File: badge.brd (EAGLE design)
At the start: 90.7 x 92.4 mm, 178 parts, among them CN4 MicroUSB, IC3 MEGA8-AI, Q1 BSS138, Q2 BSS138, T1 MMUN2133LT1G, U1 TPS61090RSAR, U2 MCP73871, U3 LIS3DHTR, U4 MIC5225-3.3, Y1 16.00MHz

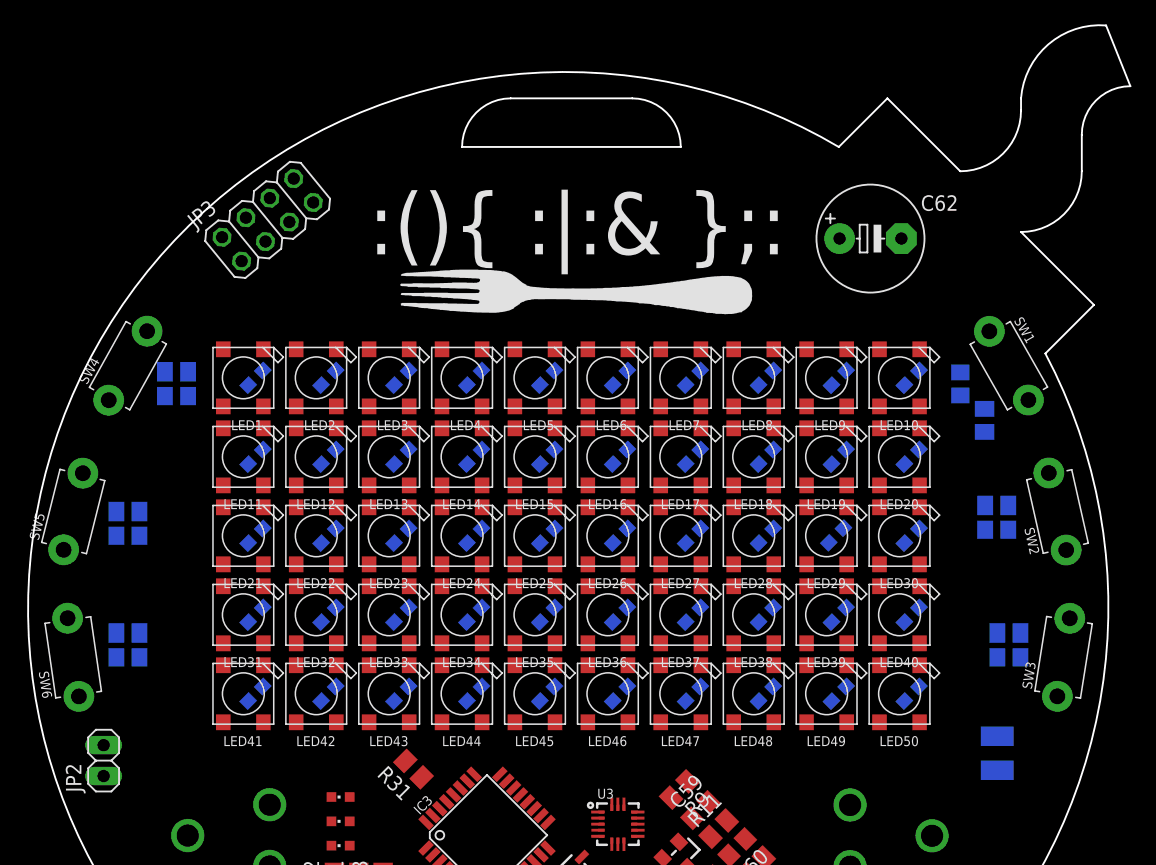
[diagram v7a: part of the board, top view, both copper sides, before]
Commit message: small silkscreen changes
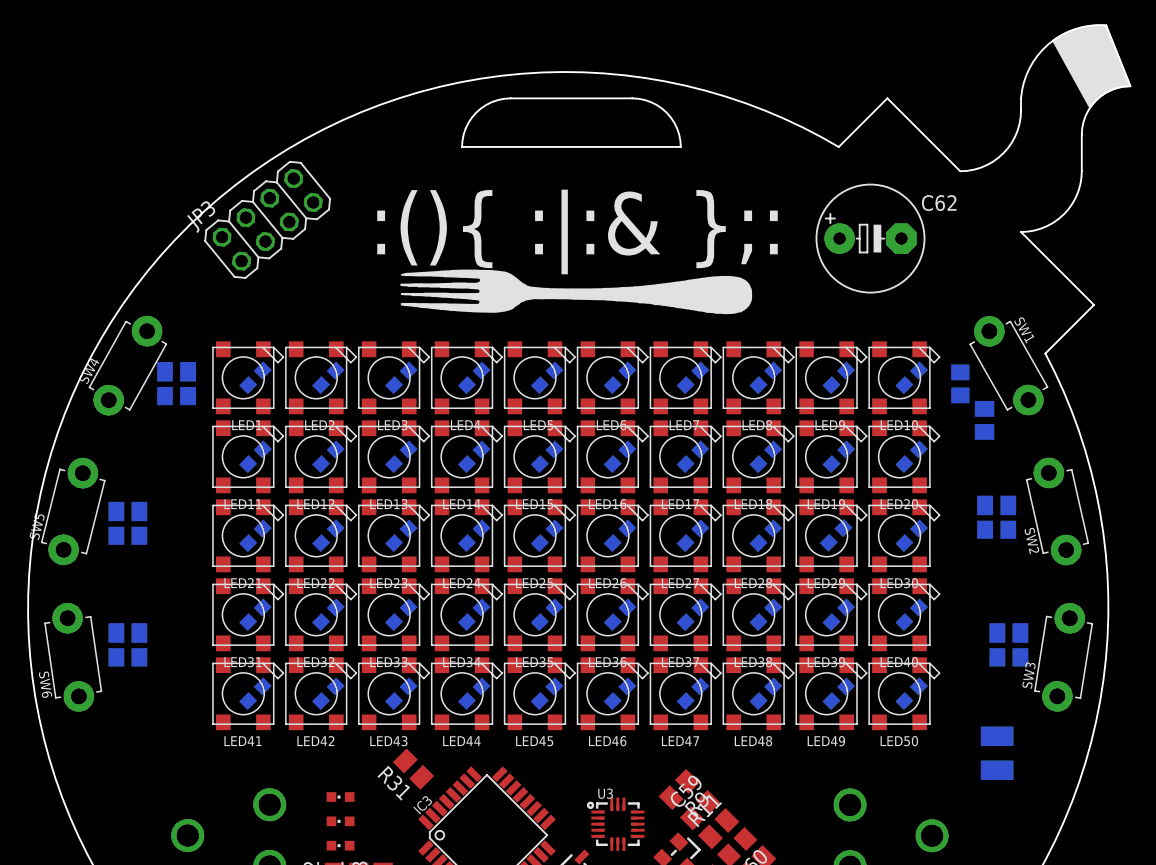
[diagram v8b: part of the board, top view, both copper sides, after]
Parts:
- removed JP2: PIEZO_HEADER, pinhead:1X02
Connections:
- net GND: no longer JP2.2
- net PIEZO: no longer JP2.1
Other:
- board text added: "fir3r007 ichorous videlen"
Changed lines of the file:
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@@
 <setting verticaltext="up"/>
 </settings>
-<grid distance="0.5" unitdist="mm" unit="mm" style="lines" multiple="1" display="yes" altdistance="5" altunitdist="mil" altunit="mil"/>
+<grid distance="0.000123031496" unitdist="mil" unit="mil" style="lines" multiple="1" display="yes" altdistance="5" altunitdist="mil" altunit="mil"/>
 <layers>
 <layer number="1" name="Top" color="4" fill="1" visible="yes" active="yes"/>
@@
 <dimension x1="0" y1="0" x2="100" y2="0" x3="50" y3="-6" textsize="1.778" layer="51"/>
 <dimension x1="100" y1="0" x2="100" y2="100" x3="105.5" y3="50" textsize="1.778" layer="51"/>
+<polygon width="0.1524" layer="21">
+<vertex x="90.002796875" y="92.986875"/>
+<vertex x="92.001878125" y="87.999740625"/>
+<vertex x="91.640853125" y="87.982459375"/>
+<vertex x="91.268303125" y="87.93445"/>
+<vertex x="90.8938375" y="87.846115625"/>
+<vertex x="90.52513125" y="87.71745"/>
+<vertex x="90.162184375" y="87.554221875"/>
+<vertex x="89.88565625" y="87.396753125"/>
+<vertex x="89.646340625" y="87.232959375"/>
+<vertex x="89.409496875" y="87.048928125"/>
+<vertex x="89.156653125" y="86.815284375"/>
+<vertex x="88.955015625" y="86.596046875"/>
+<vertex x="88.68296875" y="86.235984375"/>
+<vertex x="85.63738125" y="91.751709375"/>
+<vertex x="85.93680625" y="91.9585"/>
+<vertex x="86.259425" y="92.15668125"/>
+<vertex x="86.835534375" y="92.45165"/>
+<vertex x="87.411640625" y="92.67518125"/>
+<vertex x="87.893265625" y="92.81805625"/>
+<vertex x="88.289846875" y="92.908140625"/>
+<vertex x="88.76609375" y="92.975353125"/>
+<vertex x="89.288428125" y="93.015678125"/>
+<vertex x="89.732028125" y="93.015678125"/>
+<vertex x="90.002796875" y="92.996475"/>
+<vertex x="90.039284375" y="92.910059375"/>
+</polygon>
+<polygon width="0.1524" layer="22">
+<vertex x="89.978125" y="92.962203125"/>
+<vertex x="91.97720625" y="87.97506875"/>
+<vertex x="91.61618125" y="87.9577875"/>
+<vertex x="91.24363125" y="87.909778125"/>
+<vertex x="90.869165625" y="87.82144375"/>
+<vertex x="90.500459375" y="87.692778125"/>
+<vertex x="90.1375125" y="87.52955"/>
+<vertex x="89.860984375" y="87.37208125"/>
+<vertex x="89.62166875" y="87.2082875"/>
+<vertex x="89.384825" y="87.02425625"/>
+<vertex x="89.13198125" y="86.7906125"/>
+<vertex x="88.93034375" y="86.571375"/>
+<vertex x="88.658296875" y="86.2113125"/>
+<vertex x="85.612709375" y="91.7270375"/>
+<vertex x="85.912134375" y="91.933828125"/>
+<vertex x="86.234753125" y="92.132009375"/>
+<vertex x="86.8108625" y="92.426978125"/>
+<vertex x="87.38696875" y="92.650509375"/>
+<vertex x="87.86859375" y="92.793384375"/>
+<vertex x="88.265175" y="92.88346875"/>
+<vertex x="88.741421875" y="92.95068125"/>
+<vertex x="89.26375625" y="92.99100625"/>
+<vertex x="89.70735625" y="92.99100625"/>
+<vertex x="89.978125" y="92.971803125"/>
+<vertex x="90.0146125" y="92.8853875"/>
+</polygon>
+<text x="50.861821875" y="72.62003125" size="1.778" layer="22" font="vector" ratio="20" rot="MR0">fir3r007
+ichorous
+videlen</text>
 </plain>
 <attributes>
@@
 <element name="R19" library="resistor" library_urn="urn:adsk.eagle:library:348" package="R0805" package3d_urn="urn:adsk.eagle:package:26059/1" value="470" x="42.697571875" y="19.832134375" rot="R315"/>
 <element name="C62" library="resistor" library_urn="urn:adsk.eagle:library:348" package="E5-8,5" package3d_urn="urn:adsk.eagle:package:25860/1" value="1F" x="70.61" y="75.46"/>
-<element name="JP2" library="pinhead" library_urn="urn:adsk.eagle:library:325" package="1X02" package3d_urn="urn:adsk.eagle:package:22435/2" value="PIEZO_HEADER" x="7.5" y="32.5" rot="R90"/>
 <element name="S1" library="adafruit" library_urn="urn:adsk.eagle:library:420" package="EG1218" value="" x="58" y="6" rot="R206.5"/>
 <element name="STAT1" library="piboy_new" package="ADAFRUIT_CHIPLED_0603" value="GREEN" x="27" y="29.5" rot="R90"/>
@@
 <contactref element="C61" pad="2"/>
 <contactref element="C62" pad="-"/>
-<contactref element="JP2" pad="2"/>
 <contactref element="SW1" pad="P$1"/>
 <contactref element="SW2" pad="P$1"/>
@@
 <wire x1="10.45" y1="41" x2="20.65" y2="40.35" width="0" layer="19" extent="1-16"/>
 <wire x1="5.46354375" y1="37.783225" x2="10.45" y2="41" width="0" layer="19" extent="16-16"/>
-<wire x1="7.5" y1="33.77" x2="5.46354375" y2="37.783225" width="0" layer="19" extent="1-1"/>
-<wire x1="14.4222" y1="26.3306" x2="7.5" y2="33.77" width="0" layer="19" extent="1-1"/>
 <wire x1="8.55" y1="51" x2="10.45" y2="41" width="0" layer="19" extent="16-16"/>
 <wire x1="4.20825" y1="49.847915625" x2="8.55" y2="51" width="0" layer="19" extent="16-16"/>
+<wire x1="14.4222" y1="26.3306" x2="26.5" y2="21.55" width="0" layer="19" extent="1-1"/>
 <wire x1="23.143934375" y1="80.39595625" x2="20.65" y2="66.35" width="0" layer="19" extent="1-1"/>
 <wire x1="69.940290625" y1="11.01049375" x2="55.726865625" y2="4.86665625" width="0" layer="19" extent="1-1"/>
@@
 </signal>
 <signal name="PIEZO">
-<contactref element="JP2" pad="1"/>
 <contactref element="IC3" pad="13"/>
-<wire x1="7.5" y1="31.23" x2="42.36905" y2="23.60805" width="0" layer="19" extent="1-1"/>
 </signal>
 <signal name="SW1">
@@
 </drawing>
 <compatibility>
+<note version="6.3" minversion="6.2.2" severity="warning">
+Since Version 6.2.2 text objects can contain more than one line,
+which will not be processed correctly with this version.
+</note>
 <note version="8.2" severity="warning">
 Since Version 8.2, EAGLE supports online libraries. The ids
